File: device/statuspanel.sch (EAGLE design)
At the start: 8 parts

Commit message: Switching the resistors over to SMD components.
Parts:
- R1, R2, R3: device adafruit:R-US_0411/12 -> adafruit:R-US_R0805
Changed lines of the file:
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@@
 <grid distance="0.1" unitdist="inch" unit="inch" style="lines" multiple="1" display="no" altdistance="0.01" altunitdist="inch" altunit="inch"/>
 <layers>
-<layer number="1" name="Top" color="4" fill="1" visible="no" active="no"/>
-<layer number="2" name="Route2" color="1" fill="3" visible="no" active="no"/>
-<layer number="3" name="Route3" color="4" fill="3" visible="no" active="no"/>
-<layer number="4" name="Route4" color="1" fill="4" visible="no" active="no"/>
-<layer number="5" name="Route5" color="4" fill="4" visible="no" active="no"/>
-<layer number="6" name="Route6" color="1" fill="8" visible="no" active="no"/>
-<layer number="7" name="Route7" color="4" fill="8" visible="no" active="no"/>
-<layer number="8" name="Route8" color="1" fill="2" visible="no" active="no"/>
-<layer number="9" name="Route9" color="4" fill="2" visible="no" active="no"/>
-<layer number="10" name="Route10" color="1" fill="7" visible="no" active="no"/>
-<layer number="11" name="Route11" color="4" fill="7" visible="no" active="no"/>
-<layer number="12" name="Route12" color="1" fill="5" visible="no" active="no"/>
-<layer number="13" name="Route13" color="4" fill="5" visible="no" active="no"/>
-<layer number="14" name="Route14" color="1" fill="6" visible="no" active="no"/>
-<layer number="15" name="Route15" color="4" fill="6" visible="no" active="no"/>
-<layer number="16" name="Bottom" color="1" fill="1" visible="no" active="no"/>
-<layer number="17" name="Pads" color="2" fill="1" visible="no" active="no"/>
-<layer number="18" name="Vias" color="2" fill="1" visible="no" active="no"/>
-<layer number="19" name="Unrouted" color="6" fill="1" visible="no" active="no"/>
-<layer number="20" name="Dimension" color="15" fill="1" visible="no" active="no"/>
-<layer number="21" name="tPlace" color="14" fill="1" visible="no" active="no"/>
-<layer number="22" name="bPlace" color="7" fill="1" visible="no" active="no"/>
-<layer number="23" name="tOrigins" color="15" fill="1" visible="no" active="no"/>
-<layer number="24" name="bOrigins" color="15" fill="1" visible="no" active="no"/>
-<layer number="25" name="tNames" color="7" fill="1" visible="no" active="no"/>
-<layer number="26" name="bNames" color="7" fill="1" visible="no" active="no"/>
-<layer number="27" name="tValues" color="7" fill="1" visible="no" active="no"/>
-<layer number="28" name="bValues" color="7" fill="1" visible="no" active="no"/>
+<layer number="1" name="Top" color="4" fill="1" visible="yes" active="no"/>
+<layer number="2" name="Route2" color="16" fill="1" visible="yes" active="no"/>
+<layer number="3" name="Route3" color="4" fill="3" visible="yes" active="no"/>
+<layer number="4" name="Route4" color="1" fill="4" visible="yes" active="no"/>
+<layer number="5" name="Route5" color="4" fill="4" visible="yes" active="no"/>
+<layer number="6" name="Route6" color="1" fill="8" visible="yes" active="no"/>
+<layer number="7" name="Route7" color="4" fill="8" visible="yes" active="no"/>
+<layer number="8" name="Route8" color="1" fill="2" visible="yes" active="no"/>
+<layer number="9" name="Route9" color="4" fill="2" visible="yes" active="no"/>
+<layer number="10" name="Route10" color="1" fill="7" visible="yes" active="no"/>
+<layer number="11" name="Route11" color="4" fill="7" visible="yes" active="no"/>
+<layer number="12" name="Route12" color="1" fill="5" visible="yes" active="no"/>
+<layer number="13" name="Route13" color="4" fill="5" visible="yes" active="no"/>
+<layer number="14" name="Route14" color="1" fill="6" visible="yes" active="no"/>
+<layer number="15" name="Route15" color="23" fill="1" visible="yes" active="no"/>
+<layer number="16" name="Bottom" color="1" fill="1" visible="yes" active="no"/>
+<layer number="17" name="Pads" color="2" fill="1" visible="yes" active="no"/>
+<layer number="18" name="Vias" color="2" fill="1" visible="yes" active="no"/>
+<layer number="19" name="Unrouted" color="6" fill="1" visible="yes" active="no"/>
+<layer number="20" name="Dimension" color="24" fill="1" visible="yes" active="no"/>
+<layer number="21" name="tPlace" color="7" fill="1" visible="yes" active="no"/>
+<layer number="22" name="bPlace" color="7" fill="1" visible="yes" active="no"/>
+<layer number="23" name="tOrigins" color="15" fill="1" visible="yes" active="no"/>
+<layer number="24" name="bOrigins" color="15" fill="1" visible="yes" active="no"/>
+<layer number="25" name="tNames" color="7" fill="1" visible="yes" active="no"/>
+<layer number="26" name="bNames" color="7" fill="1" visible="yes" active="no"/>
+<layer number="27" name="tValues" color="7" fill="1" visible="yes" active="no"/>
+<layer number="28" name="bValues" color="7" fill="1" visible="yes" active="no"/>
 <layer number="29" name="tStop" color="7" fill="3" visible="no" active="no"/>
 <layer number="30" name="bStop" color="7" fill="6" visible="no" active="no"/>
@@
 <layer number="35" name="tGlue" color="7" fill="4" visible="no" active="no"/>
 <layer number="36" name="bGlue" color="7" fill="5" visible="no" active="no"/>
-<layer number="37" name="tTest" color="7" fill="1" visible="no" active="no"/>
-<layer number="38" name="bTest" color="7" fill="1" visible="no" active="no"/>
+<layer number="37" name="tTest" color="7" fill="1" visible="yes" active="no"/>
+<layer number="38" name="bTest" color="7" fill="1" visible="yes" active="no"/>
 <layer number="39" name="tKeepout" color="4" fill="11" visible="no" active="no"/>
 <layer number="40" name="bKeepout" color="1" fill="11" visible="no" active="no"/>
@@
 <layer number="44" name="Drills" color="7" fill="1" visible="no" active="no"/>
 <layer number="45" name="Holes" color="7" fill="1" visible="no" active="no"/>
-<layer number="46" name="Milling" color="3" fill="1" visible="no" active="no"/>
-<layer number="47" name="Measures" color="7" fill="1" visible="no" active="no"/>
-<layer number="48" name="Document" color="7" fill="1" visible="no" active="no"/>
-<layer number="49" name="Reference" color="7" fill="1" visible="no" active="no"/>
-<layer number="50" name="dxf" color="7" fill="1" visible="no" active="no"/>
-<layer number="51" name="tDocu" color="7" fill="1" visible="no" active="no"/>
-<layer number="52" name="bDocu" color="7" fill="1" visible="no" active="no"/>
-<layer number="53" name="tGND_GNDA" color="7" fill="9" visible="no" active="no"/>
-<layer number="54" name="bGND_GNDA" color="1" fill="9" visible="no" active="no"/>
-<layer number="56" name="wert" color="7" fill="1" visible="no" active="no"/>
-<layer number="57" name="tCAD" color="7" fill="1" visible="no" active="no"/>
-<layer number="59" name="tCarbon" color="7" fill="1" visible="no" active="no"/>
-<layer number="60" name="bCarbon" color="7" fill="1" visible="no" active="no"/>
+<layer number="46" name="Milling" color="3" fill="1" visible="yes" active="no"/>
+<layer number="47" name="Measures" color="7" fill="1" visible="yes" active="no"/>
+<layer number="48" name="Document" color="7" fill="1" visible="yes" active="no"/>
+<layer number="49" name="Reference" color="7" fill="1" visible="yes" active="no"/>
+<layer number="50" name="dxf" color="7" fill="1" visible="yes" active="no"/>
+<layer number="51" name="tDocu" color="7" fill="1" visible="yes" active="no"/>
+<layer number="52" name="bDocu" color="7" fill="1" visible="yes" active="no"/>
+<layer number="53" name="tGND_GNDA" color="7" fill="9" visible="yes" active="no"/>
+<layer number="54" name="bGND_GNDA" color="1" fill="9" visible="yes" active="no"/>
+<layer number="56" name="wert" color="7" fill="1" visible="yes" active="no"/>
+<layer number="57" name="tCAD" color="7" fill="1" visible="yes" active="no"/>
+<layer number="59" name="tCarbon" color="7" fill="1" visible="yes" active="no"/>
+<layer number="60" name="bCarbon" color="7" fill="1" visible="yes" active="no"/>
 <layer number="88" name="SimResults" color="9" fill="1" visible="yes" active="yes"/>
 <layer number="89" name="SimProbes" color="9" fill="1" visible="yes" active="yes"/>
@@
 <part name="UNPAIR" library="switch-omron" library_urn="urn:adsk.eagle:library:377" deviceset="10-XX" device="" package3d_urn="urn:adsk.eagle:package:27496/1"/>
 <part name="STAT." library="adafruit" library_urn="urn:adsk.eagle:library:420" deviceset="LED" device="3MM" package3d_urn="urn:adsk.eagle:package:6240537/1"/>
-<part name="R1" library="adafruit" library_urn="urn:adsk.eagle:library:420" deviceset="R-US_" device="0411/12" package3d_urn="urn:adsk.eagle:package:6240605/1" value="5.1"/>
-<part name="R2" library="adafruit" library_urn="urn:adsk.eagle:library:420" deviceset="R-US_" device="0411/12" package3d_urn="urn:adsk.eagle:package:6240605/1" value="4.7K"/>
-<part name="R3" library="adafruit" library_urn="urn:adsk.eagle:library:420" deviceset="R-US_" device="0411/12" package3d_urn="urn:adsk.eagle:package:6240605/1" value="4.7K"/>
+<part name="R1" library="adafruit" library_urn="urn:adsk.eagle:library:420" deviceset="R-US_" device="R0805" package3d_urn="urn:adsk.eagle:package:6240566/1" value="5.1"/>
+<part name="R2" library="adafruit" library_urn="urn:adsk.eagle:library:420" deviceset="R-US_" device="R0805" package3d_urn="urn:adsk.eagle:package:6240566/1" value="4.7K"/>
+<part name="R3" library="adafruit" library_urn="urn:adsk.eagle:library:420" deviceset="R-US_" device="R0805" package3d_urn="urn:adsk.eagle:package:6240566/1" value="4.7K"/>
 </parts>
 <sheets>

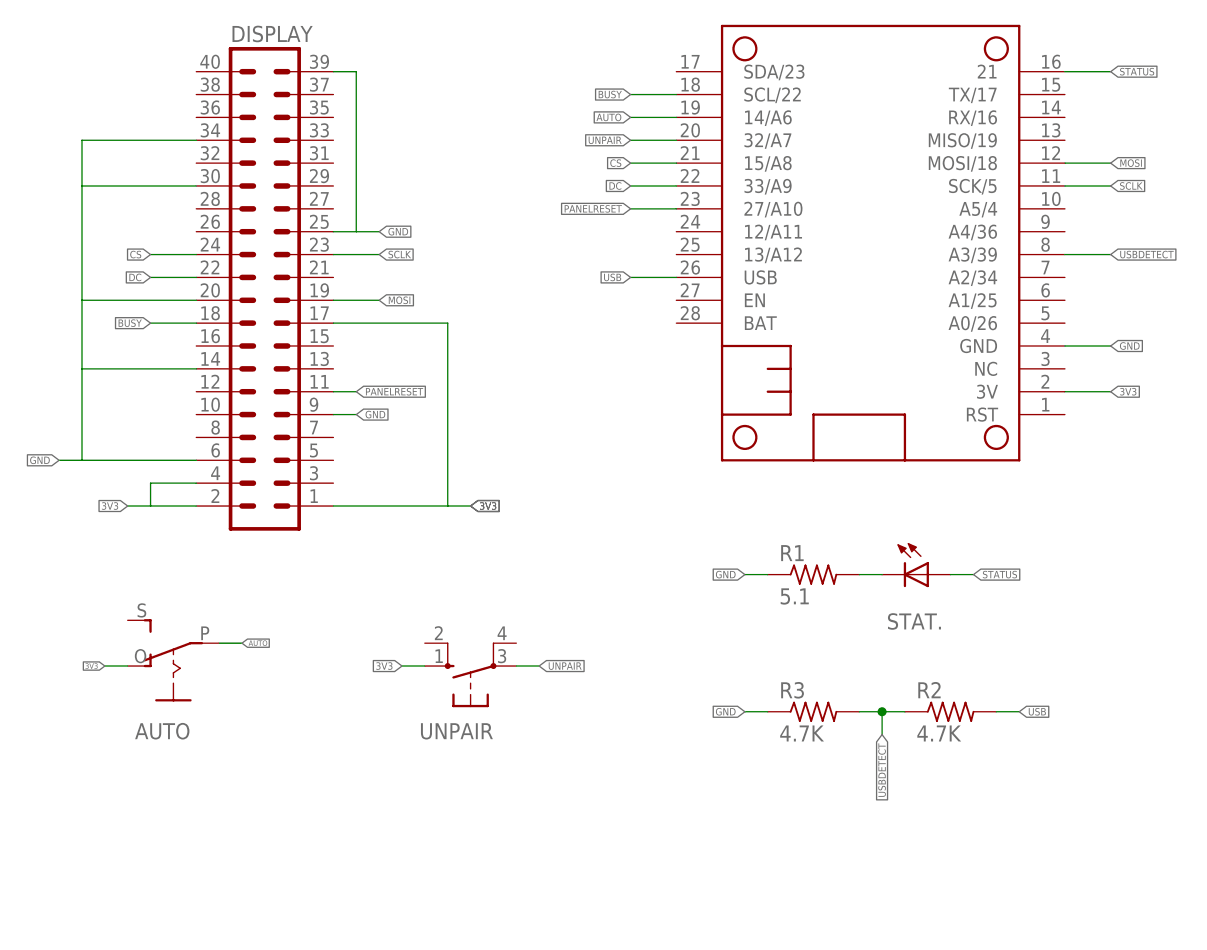
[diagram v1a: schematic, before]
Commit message: Add the reset button.
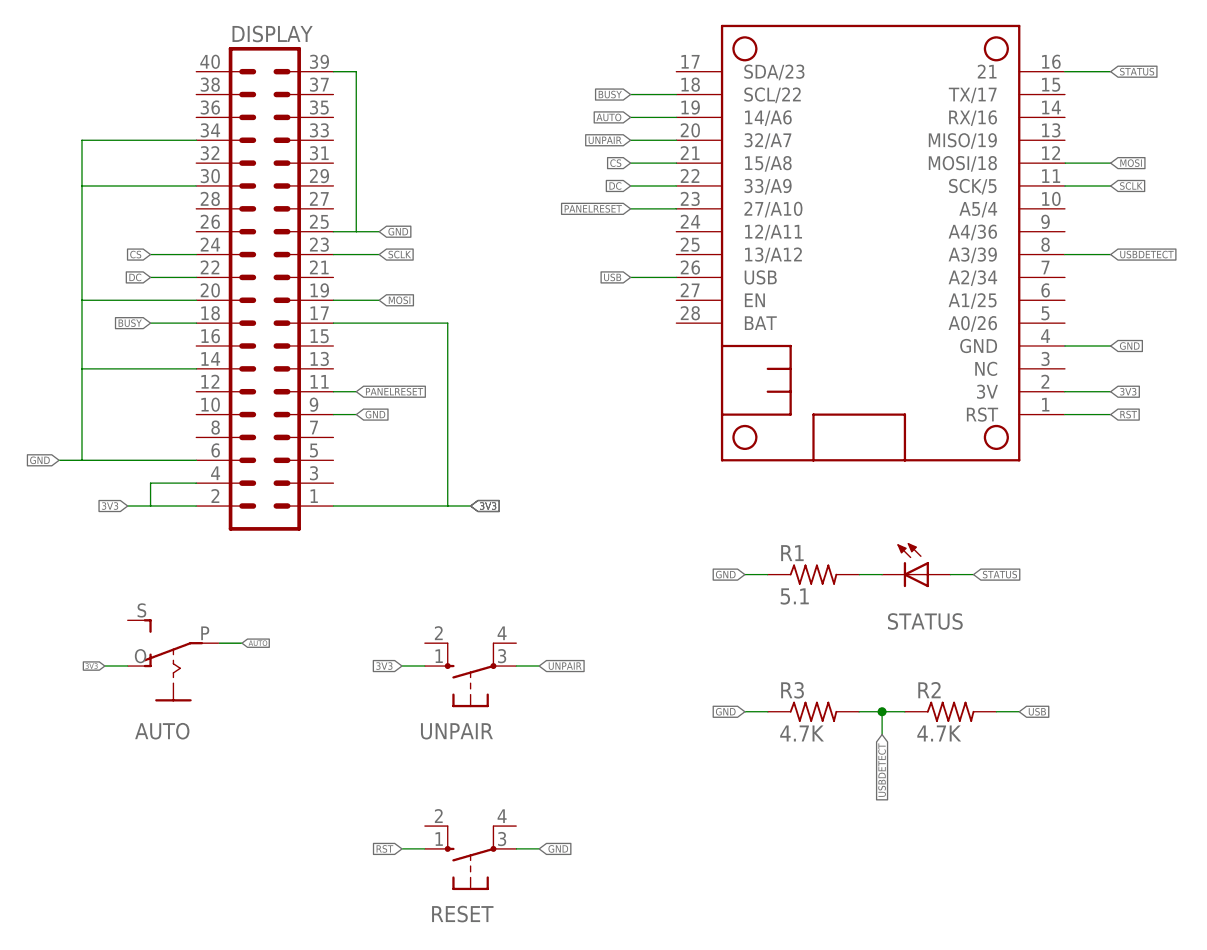
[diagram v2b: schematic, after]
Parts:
- added RESET: (no value), switch-omron:10-XX
- renumbered STAT. to STATUS
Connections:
- new net RST: HUZZAH32.RST, RESET.S
- net GND: now also RESET.P

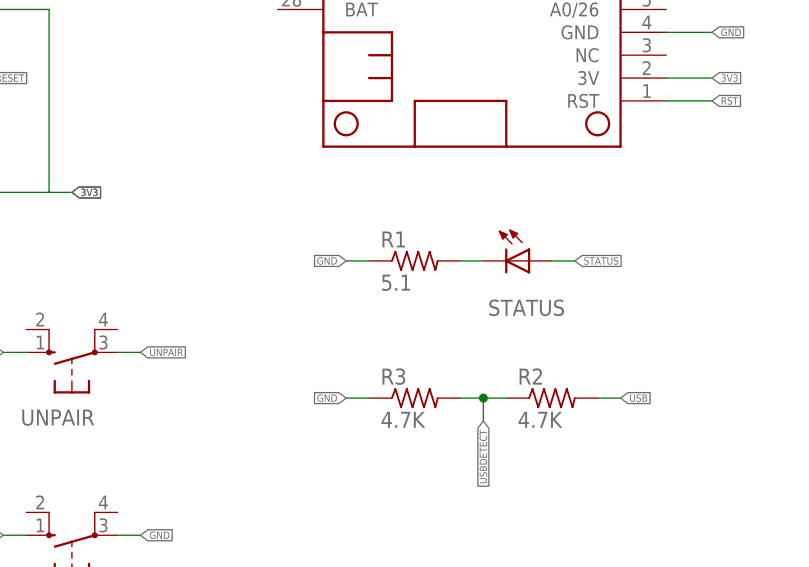
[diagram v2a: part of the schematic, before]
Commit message: Update the resistance of the LED resistor.
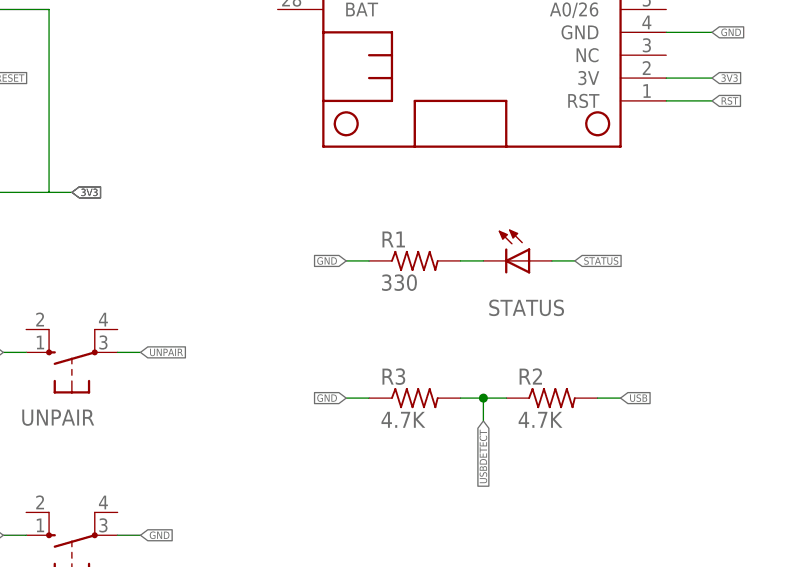
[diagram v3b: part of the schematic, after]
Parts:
- R1: value 5.1 -> 330
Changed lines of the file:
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@@
 <part name="UNPAIR" library="switch-omron" library_urn="urn:adsk.eagle:library:377" deviceset="10-XX" device="" package3d_urn="urn:adsk.eagle:package:27496/1"/>
 <part name="STATUS" library="adafruit" library_urn="urn:adsk.eagle:library:420" deviceset="LED" device="3MM" package3d_urn="urn:adsk.eagle:package:6240537/1"/>
-<part name="R1" library="adafruit" library_urn="urn:adsk.eagle:library:420" deviceset="R-US_" device="R0805" package3d_urn="urn:adsk.eagle:package:6240566/1" value="5.1"/>
+<part name="R1" library="adafruit" library_urn="urn:adsk.eagle:library:420" deviceset="R-US_" device="R0805" package3d_urn="urn:adsk.eagle:package:6240566/1" value="330"/>
 <part name="R2" library="adafruit" library_urn="urn:adsk.eagle:library:420" deviceset="R-US_" device="R0805" package3d_urn="urn:adsk.eagle:package:6240566/1" value="4.7K"/>
 <part name="R3" library="adafruit" library_urn="urn:adsk.eagle:library:420" deviceset="R-US_" device="R0805" package3d_urn="urn:adsk.eagle:package:6240566/1" value="4.7K"/>
